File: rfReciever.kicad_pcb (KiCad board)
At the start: 4 copper layers, 22.8 x 36.5 mm, 35 parts, among them J1 MOLEX 1054440001, J2 Conn_01x03, SW1 RF_RESET, SW2 RF_SLEEP, U1 TLV70130DBVR, U2 USBLC6-2SC6, U3 FT234XD-R, X1 DigiXBeeRX900Micro

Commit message: fix unconnected errors, 1 real error left?
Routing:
- net GND: track 59.9 -> 65.2 mm
- net +5V: track 22.1 -> 26.4 mm, vias 2 -> 4
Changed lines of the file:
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@@
+	)
+	(segment
+		(start 153.3 64.2)
+		(end 152.5 65)
+		(width 0.15)
+		(layer "F.Cu")
+		(net 1)
+	)
+	(segment
+		(start 154.75575 64.2)
+		(end 153.3 64.2)
+		(width 0.15)
+		(layer "F.Cu")
+		(net 1)
 	)
 	(segment
@@
 	)
 	(segment
+		(start 154.58575 58.7)
+		(end 153.91575 58.03)
+		(width 0.15)
+		(layer "F.Cu")
+		(net 1)
+	)
+	(segment
 		(start 153.85625 86.525472)
 		(end 153.85625 86.6375)
@@
 	)
 	(segment
+		(start 154.75575 58.7)
+		(end 154.58575 58.7)
+		(width 0.15)
+		(layer "F.Cu")
+		(net 1)
+	)
+	(segment
 		(start 149.75625 86.525472)
 		(end 150.498222 85.7835)
@@
 	)
 	(via
+		(at 152.5 65)
+		(size 0.6)
+		(drill 0.3)
+		(layers "F.Cu" "B.Cu")
+		(free yes)
+		(net 1)
+	)
+	(via
 		(at 142.8375 53.75)
 		(size 0.6)
@@
 		(drill 0.3)
 		(layers "F.Cu" "B.Cu")
-		(net 1)
-	)
-	(via
-		(at 152.75 65)
-		(size 0.6)
-		(drill 0.3)
-		(layers "F.Cu" "B.Cu")
-		(free yes)
 		(net 1)
 	)
@@
 	)
 	(segment
-		(start 153.55 64.2)
-		(end 152.75 65)
-		(width 0.15)
-		(layer "B.Cu")
-		(net 1)
-	)
-	(segment
 		(start 141.5816 84.710094)
 		(end 142.646506 85.775)
@@
 	)
 	(segment
+		(start 154.58575 64.2)
+		(end 153.91575 64.87)
+		(width 0.15)
+		(layer "B.Cu")
+		(net 1)
+	)
+	(segment
 		(start 137.0066 80.5532)
 		(end 138.63352 82.18012)
@@
 	)
 	(segment
+		(start 152.63 64.87)
+		(end 152.5 65)
+		(width 0.2)
+		(layer "B.Cu")
+		(net 1)
+	)
+	(segment
 		(start 142.75 86.5)
 		(end 142.75 85.878494)
@@
 	)
 	(segment
-		(start 152.75 65)
-		(end 152.88 64.87)
-		(width 0.2)
-		(layer "B.Cu")
-		(net 1)
-	)
-	(segment
-		(start 152.88 64.87)
-		(end 153.91575 64.87)
-		(width 0.2)
+		(start 154.75575 64.2)
+		(end 154.58575 64.2)
+		(width 0.15)
 		(layer "B.Cu")
 		(net 1)
@@
 	)
 	(segment
-		(start 154.75575 64.2)
-		(end 153.55 64.2)
-		(width 0.15)
-		(layer "B.Cu")
-		(net 1)
-	)
-	(segment
 		(start 142.75 85.878494)
 		(end 142.646506 85.775)
@@
 	)
 	(segment
+		(start 154.75575 58.7)
+		(end 153.2 58.7)
+		(width 0.15)
+		(layer "B.Cu")
+		(net 1)
+	)
+	(segment
+		(start 153.91575 64.87)
+		(end 152.63 64.87)
+		(width 0.2)
+		(layer "B.Cu")
+		(net 1)
+	)
+	(segment
 		(start 143.98082 85.775)
 		(end 145.00582 84.75)
@@
 		(end 136.13416 82.5532)
 		(width 0.2)
+		(layer "B.Cu")
+		(net 1)
+	)
+	(segment
+		(start 153.2 58.7)
+		(end 152.5 58)
+		(width 0.15)
 		(layer "B.Cu")
 		(net 1)
@@
 	)
 	(segment
+		(start 154.05 62.7)
+		(end 154.75575 62.7)
+		(width 0.25)
+		(layer "F.Cu")
+		(net 29)
+	)
+	(segment
+		(start 153.5 59.275)
+		(end 153.5 59.577564)
+		(width 0.25)
+		(layer "F.Cu")
+		(net 29)
+	)
+	(segment
 		(start 146.75 59.75)
 		(end 146.75 58.55)
@@
 	)
 	(segment
+		(start 153.5 59.577564)
+		(end 154.122436 60.2)
+		(width 0.25)
+		(layer "F.Cu")
+		(net 29)
+	)
+	(segment
+		(start 153.5 63.25)
+		(end 154.05 62.7)
+		(width 0.25)
+		(layer "F.Cu")
+		(net 29)
+	)
+	(segment
 		(start 145.41075 59.75)
 		(end 146.75 59.75)
@@
 		(net 29)
 	)
+	(segment
+		(start 154.122436 60.2)
+		(end 154.75575 60.2)
+		(width 0.25)
+		(layer "F.Cu")
+		(net 29)
+	)
+	(via
+		(at 153.5 59.275)
+		(size 0.6)
+		(drill 0.3)
+		(layers "F.Cu" "B.Cu")
+		(net 29)
+	)
 	(via
 		(at 152.25 59.75)
@@
 		(net 29)
 	)
-	(segment
-		(start 152.25 59.75)
+	(via
+		(at 153.5 63.25)
+		(size 0.6)
+		(drill 0.3)
+		(layers "F.Cu" "B.Cu")
+		(net 29)
+	)
+	(segment
+		(start 152.75 59.75)
 		(end 153.5 59.75)
 		(width 0.36)
+		(layer "B.Cu")
+		(net 29)
+	)
+	(segment
+		(start 153.5 59.75)
+		(end 153.5 59.275)
+		(width 0.25)
 		(layer "B.Cu")
 		(net 29)
@@
 	(segment
 		(start 152.25 59.75)
+		(end 152.75 59.75)
+		(width 0.36)
+		(layer "B.Cu")
+		(net 29)
+	)
+	(segment
+		(start 153.5 62.75)
+		(end 153.5 63.25)
+		(width 0.25)
+		(layer "B.Cu")
+		(net 29)
+	)
+	(segment
+		(start 152.25 59.75)
 		(end 152.25 62.75)
 		(width 0.36)
@@
 		(layer "B.Cu")
 		(net 29)
+	)
+	(segment
+		(start 153.475 59.25)
+		(end 153.5 59.275)
+		(width 0.36)
+		(layer "B.Cu")
+		(net 29)

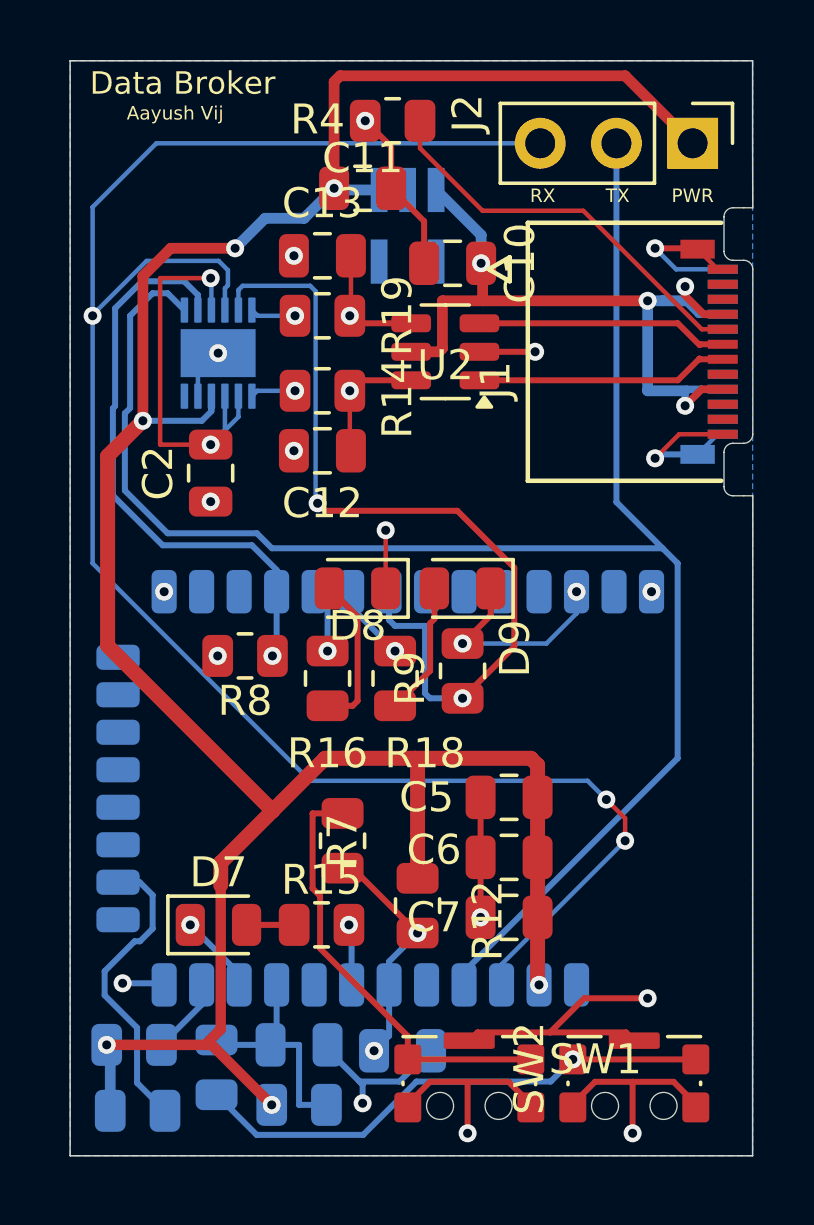
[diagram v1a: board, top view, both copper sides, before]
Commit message: Minor updates (test points, silkscreen, traces)
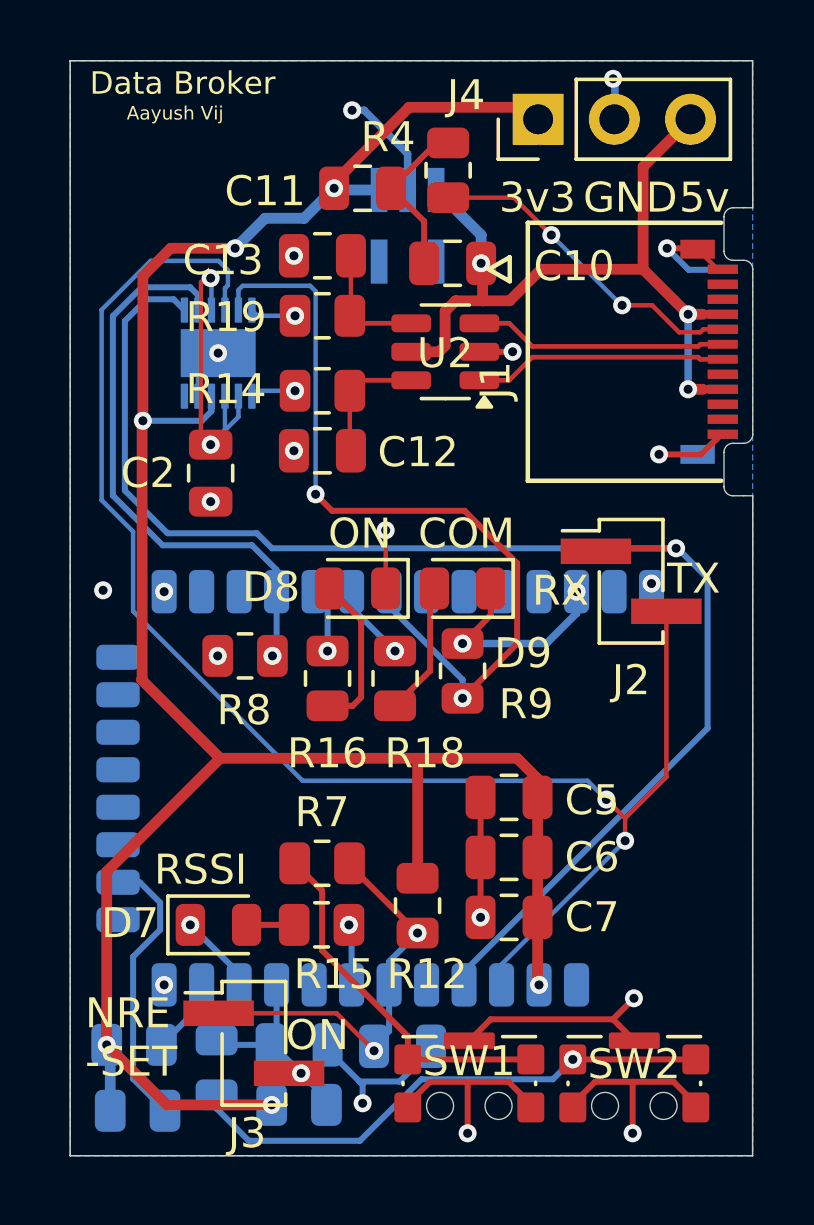
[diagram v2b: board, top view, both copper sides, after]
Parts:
- added J3: Conn_01x02, Connector_PinHeader_2.00mm:PinHeader_1x02_P2.00mm_Vertical_SMD_Pin1Left, F.Cu at (139.1, 84.5)
- added J4: Conn_01x03, Connector_PinHeader_2.54mm:PinHeader_1x03_P2.54mm_Vertical, F.Cu at (148.6, 53.7)
- added R1: 27, rfReciever-Footprints:stockBroker, B.Cu at (147.6, 62.5)
- added R2: 27, rfReciever-Footprints:RFHazard, B.Cu at (137.8, 55.4)
- added R5: 27, rfReciever-Footprints:emWave, B.Cu at (137.5, 65.8)
- J2: value Conn_01x03 -> Conn_01x02; footprint Connector_PinHeader_2.54mm:PinHeader_1x03_P2.54mm_Vertical -> Connector_PinHeader_2.00mm:PinHeader_1x02_P2.00mm_Vertical_SMD_Pin1Left
- moved J2 14.7 mm to (151.7, 69.1), turned to 0 degrees
- moved R4 2.48 mm to (145.6, 55.4), turned to 90 degrees
- moved R7 1.01 mm to (141.4, 78.5), turned to 180 degrees
- moved C8 0.15 mm to (144.1, 84.6)
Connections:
- net Net-(J1-CC) renamed /USB_Identifier
- J2 pad 1: +3.3V -> /RF_TXD
- J2 pad 2: /RF_TXD -> /RF_RXD
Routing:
- net /RF_RXD: track 63.0 -> 50.9 mm, vias 3 -> 2
- net /RF_TXD: track 58.8 -> 48.4 mm, vias 0 -> 1
- net +3.3V: track 87.9 -> 80.0 mm
- net /RF_RESET: track 7.92 -> 13.6 mm
- net /FTDI_RESET: track 13.1 -> 10.1 mm
- net /USB_Identifier: track 13.5 -> 11.1 mm, vias 0 -> 2
- net /RF_SW_RESET: track 15.1 -> 12.6 mm
- net +5V: track 26.4 -> 28.8 mm, vias 4 -> 3
- net GND: track 65.2 -> 63.7 mm, vias 21 -> 23
- net /UART_CTS: track 28.8 -> 27.6 mm
- net /RF_SLEEP: track 7.87 -> 6.82 mm, vias 0 -> 1
- net Net-(X1-SPI_N_SSEL/DIO17): track 10.1 -> 9.44 mm
- net /USB_OUT_D+: vias 1 -> 0
- net /USB_OUT_D-: vias 1 -> 0
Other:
- board text added: "3v3"
- board text added: "5v"
- board text added: "COM"
- board text added: "GND"
- board text added: "NRE -SET"
- board text added: "ON"
- board text added: "RSSI"
- board text removed: "PWR"

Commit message: More minor tweaks + silkscreen
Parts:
- removed R1: 27, rfReciever-Footprints:stockBroker
- removed R2: 27, rfReciever-Footprints:RFHazard
- removed R5: 27, rfReciever-Footprints:emWave
- added LOGO1: Stock Broker, rfReciever-Footprints:stockBroker, B.Cu at (147.6, 62.3)
- added LOGO2: RF Hazard, rfReciever-Footprints:RFHazard, B.Cu at (137.7, 55.4)
- added LOGO3: EM Wave, rfReciever-Footprints:emWave, B.Cu at (137.5, 65.8)

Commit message: fixed drc
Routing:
- net GND: track 63.7 -> 35.7 mm
- net /RF_RXD: track 50.9 -> 36.3 mm
- net /RF_TXD: track 48.4 -> 49.4 mm, vias 1 -> 2
- net +5V: track 28.8 -> 29.7 mm
- net +3.3V: track 80.0 -> 79.2 mm
